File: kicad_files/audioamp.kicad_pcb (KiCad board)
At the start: 2 copper layers, 43 parts, among them J1 Conn_01x03_Female, J2 Conn_01x02_Female, U1 TDA2030, U2 TDA2030, U3 TL084

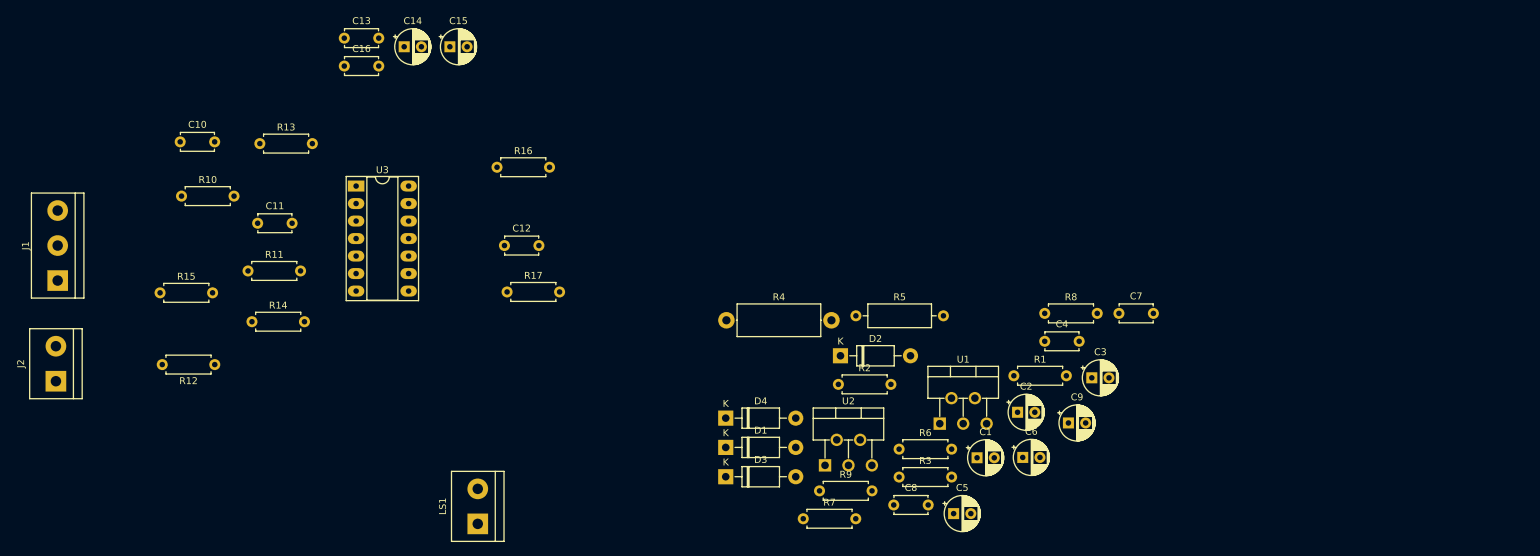
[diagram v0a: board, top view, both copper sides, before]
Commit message: Roteado o filtro passa-baixas, 1 jumper usado
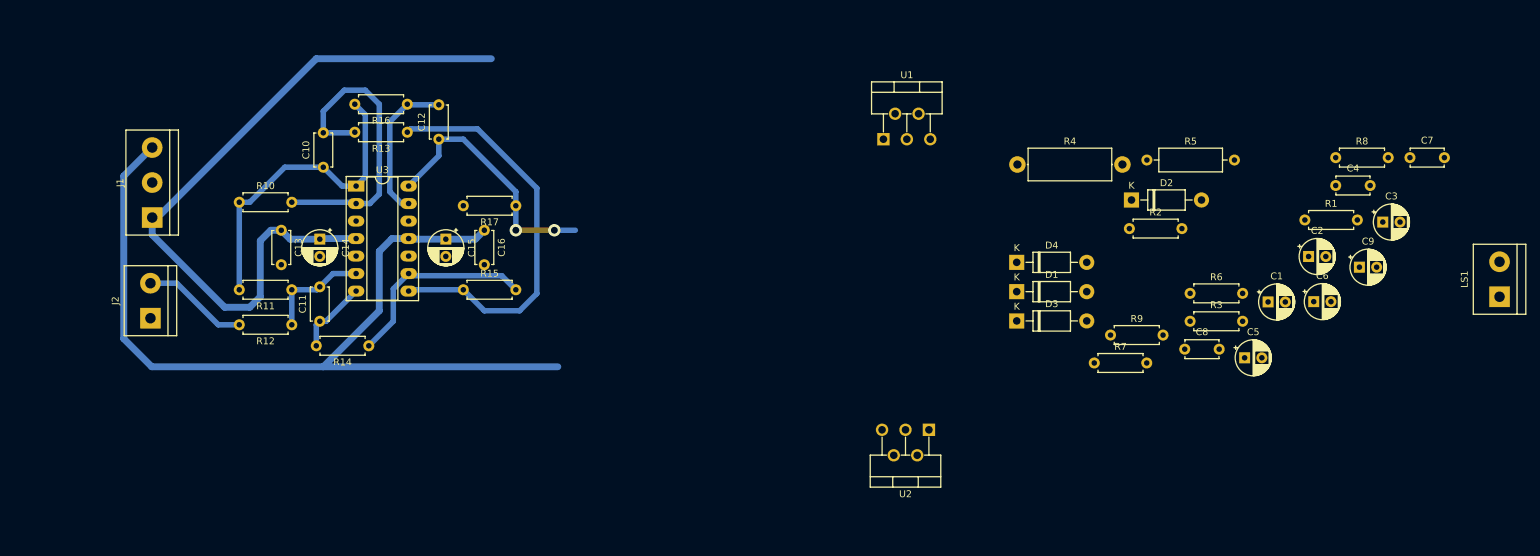
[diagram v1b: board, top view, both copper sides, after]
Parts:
- moved LS1 151.9 mm to (243.8, 91.4)
- moved D2 47.9 mm to (190.4, 77.4)
- moved C2 47.9 mm to (216.1, 85.6)
- moved C3 47.9 mm to (226.9, 80.6)
- moved C6 47.9 mm to (216.9, 92.1)
- moved C9 47.9 mm to (223.5, 87.1)
- moved R5 47.9 mm to (192.7, 71.6)
- moved C1 47.9 mm to (210.2, 92.2)
- moved C4 47.9 mm to (220.1, 75.3)
- moved C5 47.9 mm to (206.8, 100.3)
- moved C7 47.9 mm to (230.8, 71.2)
- moved C8 47.9 mm to (198.2, 99.0)
- moved D1 47.9 mm to (173.8, 90.7)
- moved D3 47.9 mm to (173.8, 94.9)
- moved D4 47.9 mm to (173.8, 86.4)
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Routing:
- net -VDC: track 0.00 -> 130.8 mm
- net +VDC: track 0.00 -> 105.2 mm
- net Net-(R13-Pad1): track 0.00 -> 58.8 mm
- net /Filtro Passa-Baixas/Vo1: track 0.00 -> 45.9 mm
- net Net-(C10-Pad2): track 0.00 -> 44.4 mm
- net /+SIG_F: track 0.00 -> 37.2 mm, vias 0 -> 2
- net Net-(R14-Pad1): track 0.00 -> 29.4 mm
- net Net-(C12-Pad2): track 0.00 -> 21.8 mm
- net /+SIG: track 0.00 -> 15.4 mm
- net Net-(C11-Pad2): track 0.00 -> 15.4 mm
- net Net-(C11-Pad1): track 0.00 -> 10.9 mm
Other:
- net class Default: clearance 0.2 -> 0.3; trace_width 0.25 -> 0.8; via_dia 0.8 -> 1.8; via_drill 0.4 -> 1
- net class Power added: clearance 0.4, trace_width 1, via_dia 1.8, via_drill 1
- rule trace_clearance: 0.2 -> 0.3

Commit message: Roteado o amplificador, 1 jumper usado no total
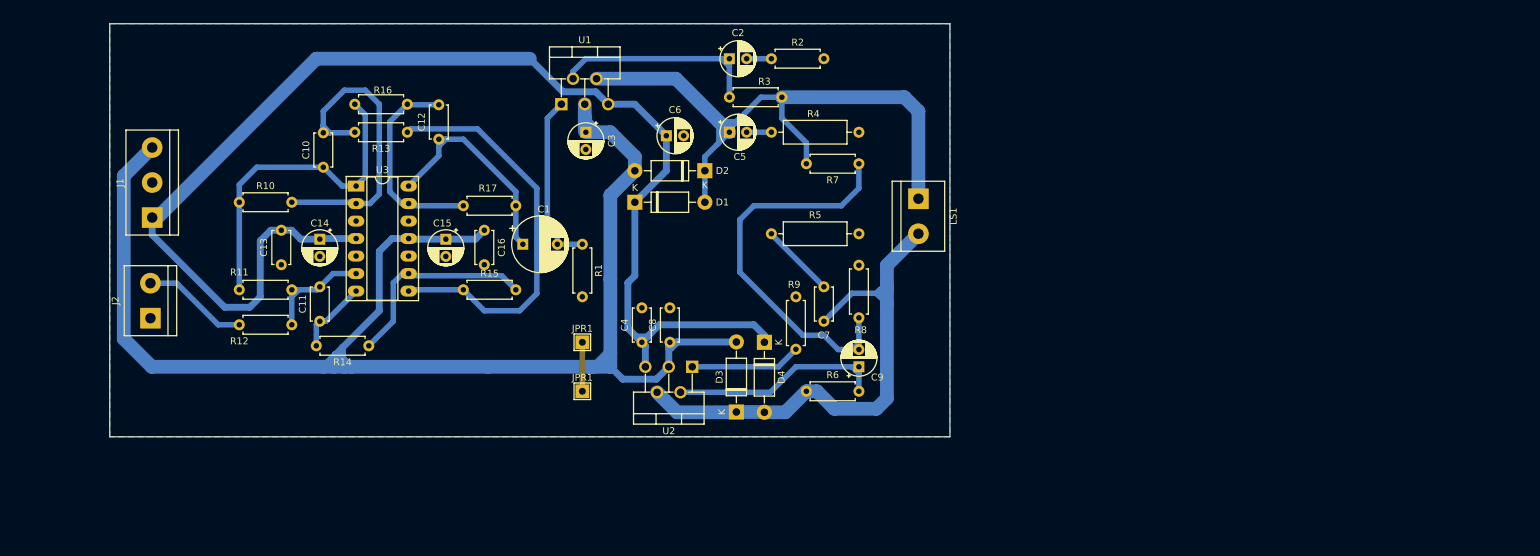
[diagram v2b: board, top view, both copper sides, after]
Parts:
- added JPR1: TestPoint_THTPad_2.0x2.0mm_Drill1.0mm, TestPoint:TestPoint_THTPad_2.0x2.0mm_Drill1.0mm, F.Cu at (110.7, 98.0)
- added JPR1: TestPoint_THTPad_2.0x2.0mm_Drill1.0mm, TestPoint:TestPoint_THTPad_2.0x2.0mm_Drill1.0mm, F.Cu at (110.7, 105.2)
- C1: footprint Capacitor_THT:CP_Radial_D5.0mm_P2.50mm -> Capacitor_THT:CP_Radial_D8.0mm_P5.00mm
- R4: footprint Resistor_THT:R_Axial_DIN0414_L11.9mm_D4.5mm_P15.24mm_Horizontal -> Resistor_THT:R_Axial_DIN0309_L9.0mm_D3.2mm_P12.70mm_Horizontal
- moved C3 116.4 mm to (111.3, 67.6), turned to 270 degrees
- moved C1 108.5 mm to (102.1, 83.8)
- moved R1 104.9 mm to (110.7, 83.8), turned to 270 degrees
- moved C4 103.2 mm to (119.4, 98.0), turned to 90 degrees
- moved C6 97.0 mm to (122.9, 68.1)
- moved C2 88.8 mm to (132.1, 56.9)
- moved C7 88.3 mm to (145.8, 95.0), turned to 90 degrees
- moved LS1 85.5 mm to (159.5, 77.2), turned to 270 degrees
- moved C5 81.6 mm to (132.1, 67.6)
- moved C8 74.7 mm to (123.4, 98.0), turned to 90 degrees
- moved C9 74.1 mm to (150.9, 101.6), turned to 90 degrees
- moved R8 73.0 mm to (150.9, 94.5), turned to 90 degrees
- moved R3 67.6 mm to (139.7, 62.5), turned to 180 degrees
- moved D2 62.0 mm to (128.5, 73.2), turned to 180 degrees
- moved R2 57.5 mm to (138.2, 56.9)
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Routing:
- net /OUT+: track 0.00 -> 98.9 mm
- net -VDC: track 130.8 -> 223.0 mm
- net +VDC: track 105.2 -> 194.1 mm
- net /OUT-: track 0.00 -> 79.9 mm
- net Net-(C9-Pad2): track 0.00 -> 58.3 mm
- net /T2-: track 0.00 -> 32.4 mm
- net /T2+: track 0.00 -> 31.7 mm
- net /T1+: track 0.00 -> 25.4 mm
- net /T1-: track 0.00 -> 16.1 mm
- net Net-(C7-Pad2): track 0.00 -> 10.9 mm
- net Net-(C12-Pad2): track 21.8 -> 29.9 mm
- net GND: track 0.00 -> 7.11 mm
- net /+SIG_F: track 37.2 -> 32.4 mm, vias 2 -> 0
- net Net-(C5-Pad2): track 0.00 -> 3.60 mm
- net Net-(C2-Pad2): track 0.00 -> 3.60 mm
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- added copper zone on B.Cu, net GND
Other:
- board outline added: 121.9 x 59.9 mm

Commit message: Alguns componentes movidos para melhorar a organização, ainda um jumper usado
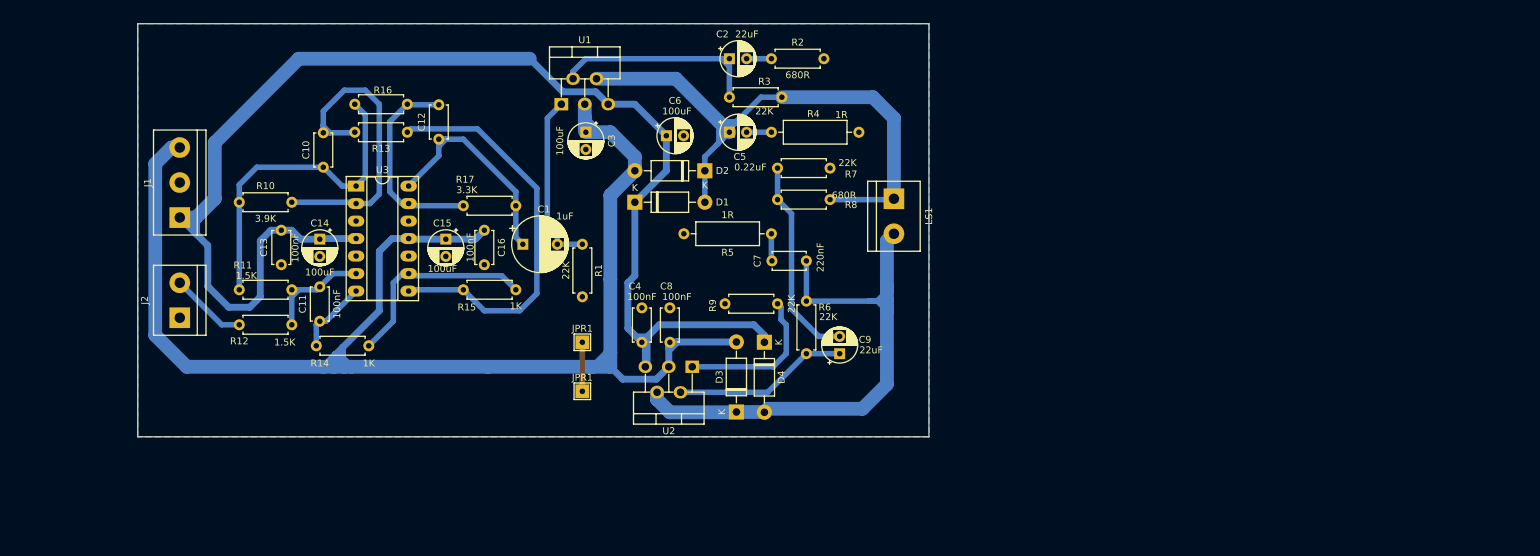
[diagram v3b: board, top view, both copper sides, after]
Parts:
- moved R8 24.7 mm to (139.1, 72.8), turned to 0 degrees
- moved R6 13.1 mm to (143.3, 92.1), turned to 270 degrees
- moved R7 12.9 mm to (139.1, 77.3), turned to 0 degrees
- moved C7 9.12 mm to (143.3, 86.2), turned to 180 degrees
- moved R9 7.12 mm to (139.1, 92.5), turned to 180 degrees
- moved J2 4.25 mm to (52.3, 94.5)
- moved J1 4.00 mm to (52.3, 79.9)
- moved LS1 3.56 mm to (156.0, 77.2)
- moved C9 3.38 mm to (148.1, 99.7)
- turned R5 to 180 degrees
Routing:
- net Net-(C9-Pad2): track 58.3 -> 29.9 mm
- net +VDC: track 194.1 -> 201.9 mm
- net /T2-: track 32.4 -> 25.4 mm
- net Net-(C7-Pad2): track 10.9 -> 4.05 mm
- net /T1-: track 16.1 -> 22.2 mm
- net /OUT+: track 98.9 -> 92.9 mm
- net /OUT-: track 79.9 -> 85.0 mm
- net -VDC: track 223.0 -> 218.6 mm
- net /+SIG: track 15.4 -> 11.2 mm
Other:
- board size 121.9 x 59.9 mm -> 114.8 x 59.9 mm

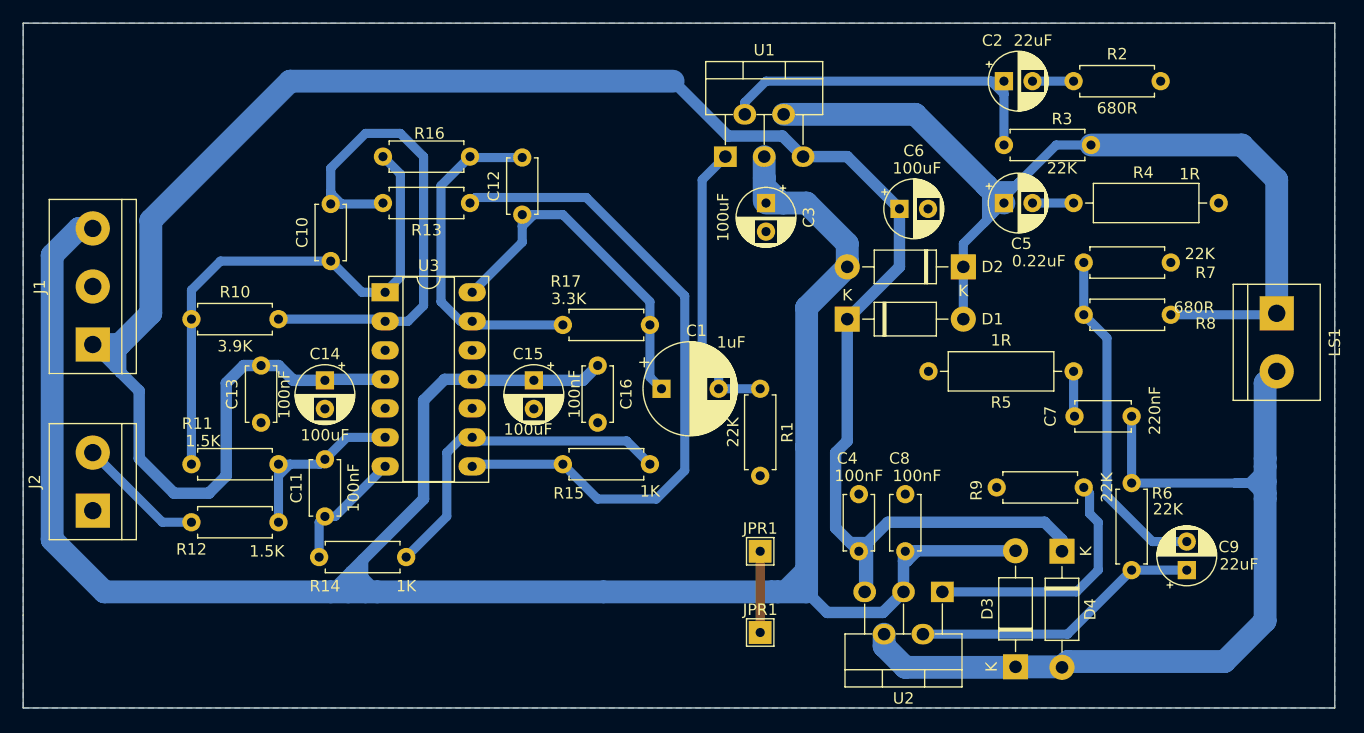
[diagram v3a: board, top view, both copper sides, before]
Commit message: Adicionados buracos de parafusos e gerados gerbers
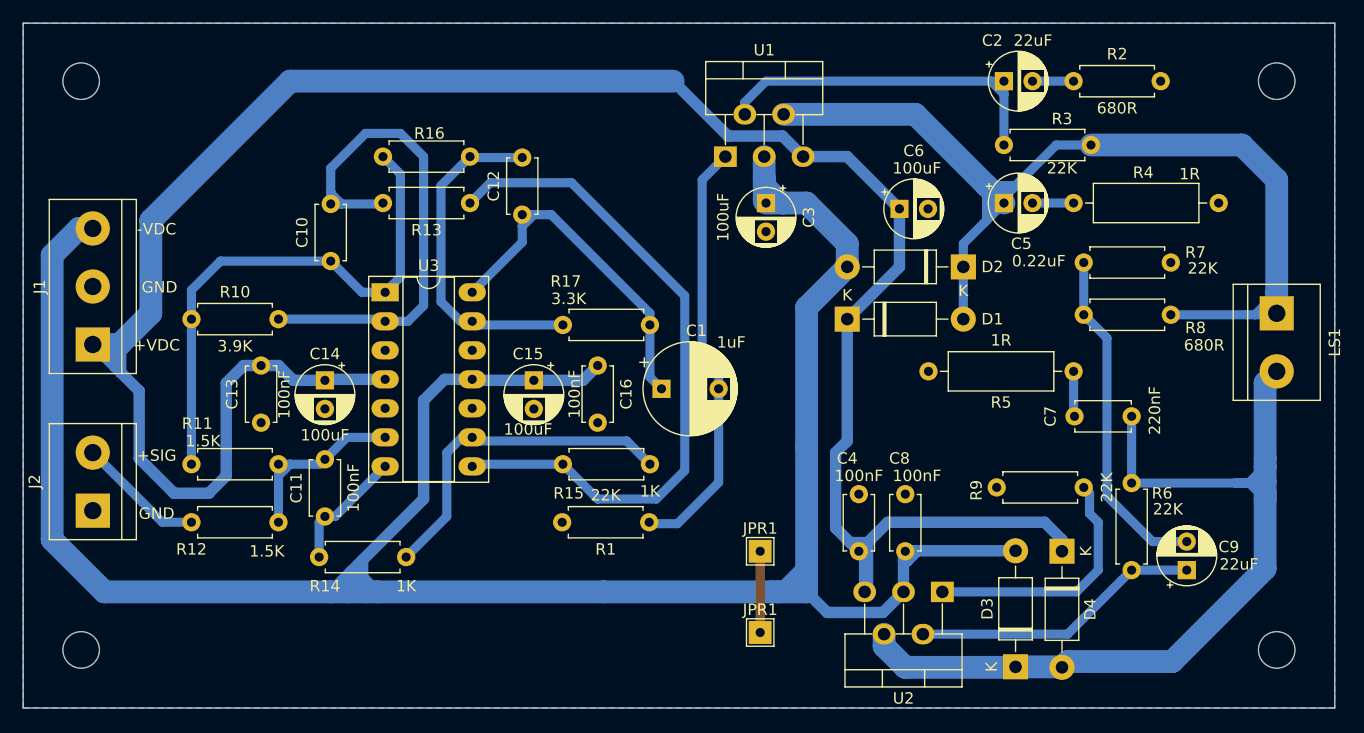
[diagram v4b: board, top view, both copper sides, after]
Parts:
- added REF**: MountingHole_3.2mm_M3, MountingHole:MountingHole_3.2mm_M3, F.Cu at (156.0, 56.9)
- added REF**: MountingHole_3.2mm_M3, MountingHole:MountingHole_3.2mm_M3, F.Cu at (156.0, 106.7)
- added REF**: MountingHole_3.2mm_M3, MountingHole:MountingHole_3.2mm_M3, F.Cu at (51.3, 106.7)
- added REF**: MountingHole_3.2mm_M3, MountingHole:MountingHole_3.2mm_M3, F.Cu at (51.3, 56.9)
- moved R1 15.2 mm to (101.0, 95.5), turned to 180 degrees
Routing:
- net /T1+: track 25.4 -> 37.5 mm
- net /OUT+: track 92.9 -> 95.6 mm
- net /OUT-: track 85.0 -> 82.3 mm
- net Net-(R13-Pad1): track 58.8 -> 60.6 mm
- net /+SIG_F: track 32.4 -> 31.8 mm
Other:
- board text added: "+SIG"
- board text added: "+VDC"
- board text added: "-VDC"
- board text added: "GND"
